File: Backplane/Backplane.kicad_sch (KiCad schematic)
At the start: 33 parts, among them J10 Conn_01x02, J11 Conn_01x02, J12 Conn_02x12_Odd_Even, J13 Conn_01x02, J14 Conn_01x02, J15 Conn_01x02, J16 Conn_01x02, J17 Conn_01x02, J18 Conn_01x02, J19 Conn_01x02_Pin, J20 Conn_01x02_Pin, J21 Conn_01x02_Pin, J22 Conn_01x02_Pin, J23 Conn_01x02_Pin, J24 Conn_01x02_Pin, J25 Conn_01x02_Pin, J26 Conn_01x02_Pin, J27 Conn_01x02, J5 Conn_01x02, J6 1720420202, J7 Conn_01x02, J8 Conn_01x02, J9 Conn_01x02

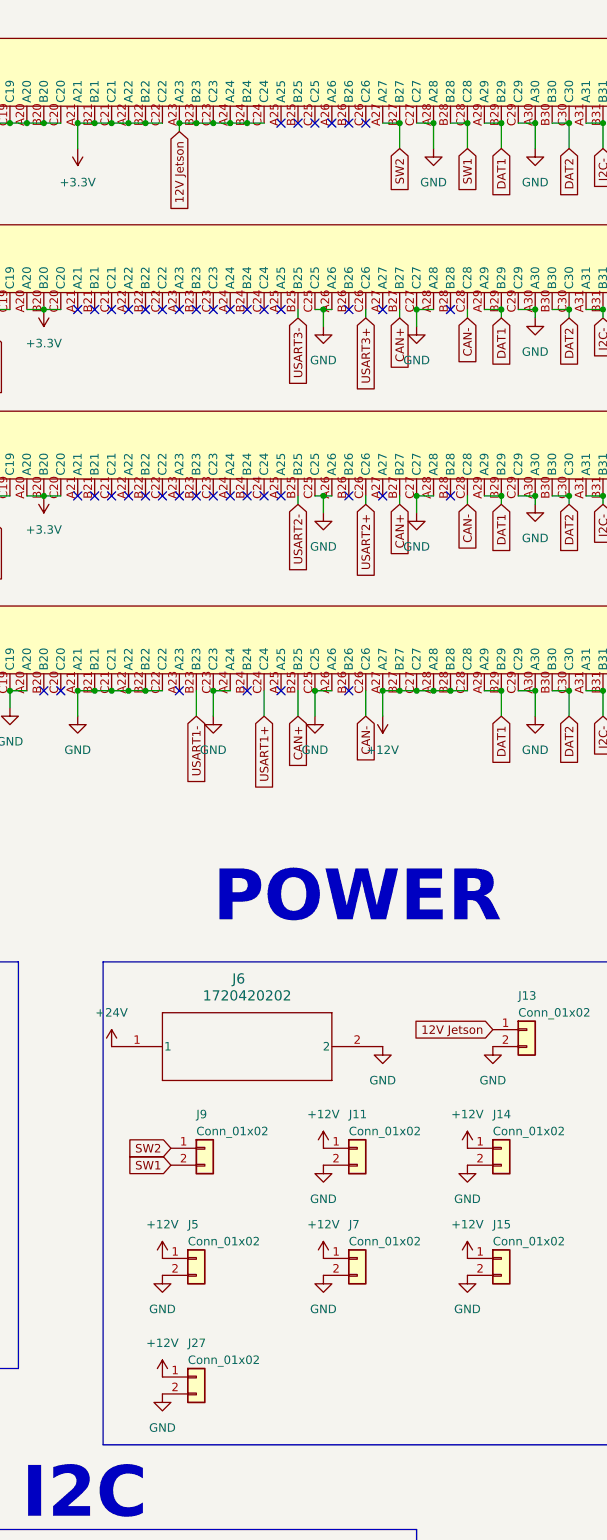
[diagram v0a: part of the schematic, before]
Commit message: Changed Backplane and Power Card for proper connection between the killswitches in the new system
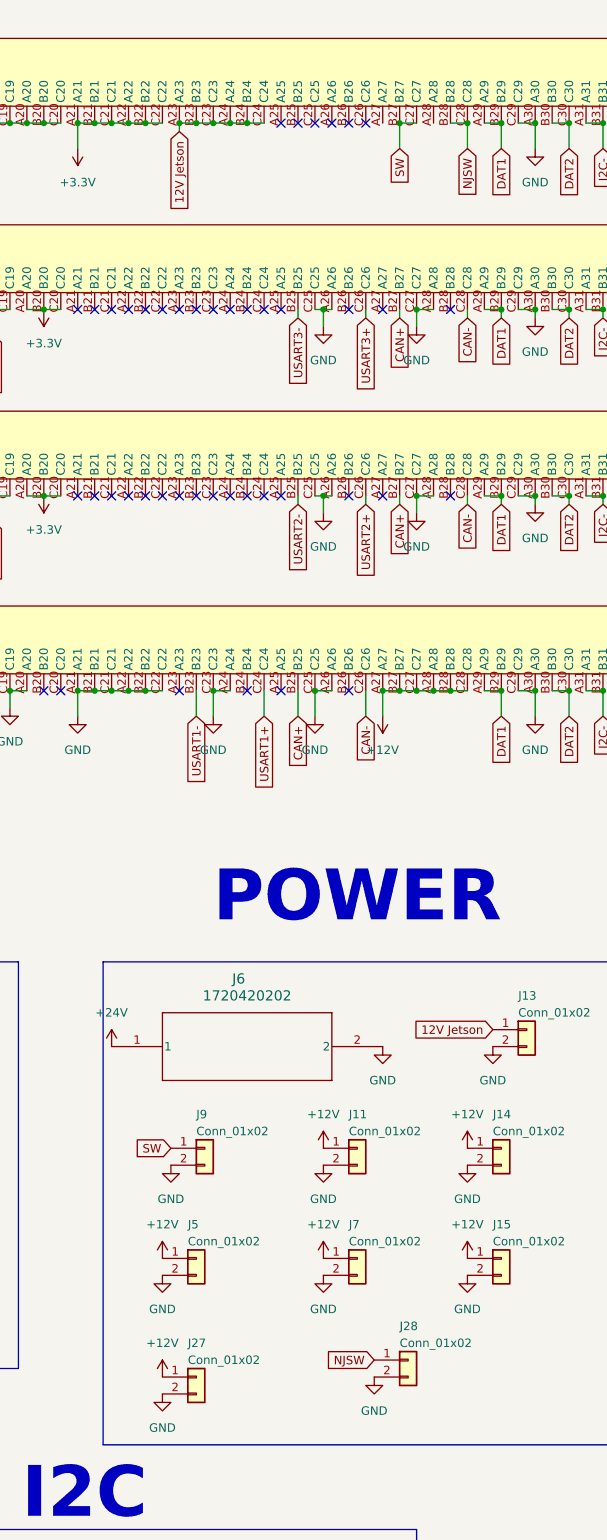
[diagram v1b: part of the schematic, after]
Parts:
- added J28: Conn_01x02, Connector_JST:JST_PH_B2B-PH-K_1x02_P2.00mm_Vertical, symbol Connector_Generic:Conn_01x02
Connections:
- net GND: now also J9.2 (Pin_2), J28.2 (Pin_2); no longer J1.A28, J1.C27
- net SW1 renamed NJSW
- net NJSW: now also J28.1 (Pin_1); no longer J9.2 (Pin_2)
- net SW2 renamed SW
- net SW: now also J1.C27; no longer J1.A27
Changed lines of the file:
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@@
 	)
 	(junction
-		(at 232.41 34.29)
-		(diameter 0)
-		(color 0 0 0 0)
-	)
-	(junction
 		(at 80.01 62.23)
 		(diameter 0)
@@
 	)
 	(junction
+		(at 232.41 34.29)
+		(diameter 0)
+		(color 0 0 0 0)
+	)
+	(junction
 		(at 273.05 62.23)
 		(diameter 0)
@@
 	)
 	(junction
-		(at 237.49 34.29)
-		(diameter 0)
-		(color 0 0 0 0)
-	)
-	(junction
 		(at 209.55 34.29)
 		(diameter 0)
@@
 	(wire
 		(pts
-			(xy 229.87 34.29) (xy 232.41 34.29)
-		)
-		(stroke
-			(width 0)
-			(type default)
-		)
-	)
-	(wire
-		(pts
 			(xy 95.25 90.17) (xy 97.79 90.17)
 		)
@@
 	(wire
 		(pts
-			(xy 234.95 34.29) (xy 237.49 34.29)
-		)
-		(stroke
-			(width 0)
-			(type default)
-		)
-	)
-	(wire
-		(pts
 			(xy 57.15 34.29) (xy 59.69 34.29)
 		)
@@
 	(wire
 		(pts
-			(xy 237.49 34.29) (xy 237.49 38.1)
-		)
-		(stroke
-			(width 0)
-			(type default)
-		)
-	)
-	(wire
-		(pts
 			(xy 295.91 195.58) (xy 297.18 195.58)
 		)
@@
 	(wire
 		(pts
+			(xy 232.41 34.29) (xy 234.95 34.29)
+		)
+		(stroke
+			(width 0)
+			(type default)
+		)
+	)
+	(wire
+		(pts
 			(xy 59.69 62.23) (xy 62.23 62.23)
 		)
@@
 		)
 	)
-	(global_label "SW1"
+	(global_label "NJSW"
 		(shape input)
 		(at 242.57 38.1 270)
@@
 		)
 		(property "Intersheetrefs" "${INTERSHEET_REFS}"
-			(at 242.57 44.9556 90)
+			(at 242.57 46.0442 90)
 			(effects
 				(font
@@
 		)
 	)
-	(global_label "SW2"
+	(global_label "SW"
 		(shape input)
 		(at 198.12 187.96 180)
@@
 		)
 		(property "Intersheetrefs" "${INTERSHEET_REFS}"
-			(at 191.2644 187.96 0)
+			(at 192.4739 187.96 0)
 			(effects
 				(font
@@
 		)
 	)
-	(global_label "SW1"
-		(shape input)
-		(at 198.12 190.5 180)
-		(fields_autoplaced yes)
-		(effects
-			(font
-				(size 1.27 1.27)
-			)
-			(justify right)
-		)
-		(property "Intersheetrefs" "${INTERSHEET_REFS}"
-			(at 191.2644 190.5 0)
-			(effects
-				(font
-					(size 1.27 1.27)
-				)
-				(justify right)
-				(hide yes)
-			)
-		)
-	)
 	(global_label "I2C-"
 		(shape input)
@@
 		)
 	)
-	(global_label "SW2"
+	(global_label "SW"
 		(shape input)
 		(at 232.41 38.1 270)
@@
 		)
 		(property "Intersheetrefs" "${INTERSHEET_REFS}"
-			(at 232.41 44.9556 90)
+			(at 232.41 43.7461 90)
 			(effects
 				(font
@@
 		)
 	)
+	(global_label "NJSW"
+		(shape input)
+		(at 228.6 219.71 180)
+		(fields_autoplaced yes)
+		(effects
+			(font
+				(size 1.27 1.27)
+			)
+			(justify right)
+		)
+		(property "Intersheetrefs" "${INTERSHEET_REFS}"
+			(at 220.6558 219.71 0)
+			(effects
+				(font
+					(size 1.27 1.27)
+				)
+				(justify right)
+				(hide yes)
+			)
+		)
+	)
 	(global_label "DAT2"
 		(shape input)
@@
 	)
 	(symbol
-		(lib_id "power:GND")
-		(at 237.49 38.1 0)
-		(unit 1)
-		(exclude_from_sim no)
-		(in_bom yes)
-		(on_board yes)
-		(dnp no)
-		(fields_autoplaced yes)
-		(property "Reference" "#PWR038"
-			(at 237.49 44.45 0)
-			(effects
-				(font
-					(size 1.27 1.27)
-				)
-				(hide yes)
-			)
-		)
-		(property "Value" "GND"
-			(at 237.49 43.18 0)
-			(effects
-				(font
-					(size 1.27 1.27)
-				)
-			)
-		)
-		(property "Footprint" ""
-			(at 237.49 38.1 0)
-			(effects
-				(font
-					(size 1.27 1.27)
-				)
-				(hide yes)
-			)
-		)
-		(property "Datasheet" ""
-			(at 237.49 38.1 0)
-			(effects
-				(font
-					(size 1.27 1.27)
-				)
-				(hide yes)
-			)
-		)
-		(property "Description" ""
-			(at 237.49 38.1 0)
-			(effects
-				(font
-					(size 1.27 1.27)
-				)
-				(hide yes)
-			)
-		)
-		(pin "1"
-		)
-		(instances
-			(project "Backplane"
-				(path "/73356aaf-05d8-4115-a1e4-2bd56b8d572b"
-					(reference "#PWR038")
-					(unit 1)
-				)
-			)
-		)
-	)
-	(symbol
 		(lib_name "GND_1")
 		(lib_id "power:GND")
@@
 	)
 	(symbol
+		(lib_name "GND_2")
+		(lib_id "power:GND")
+		(at 198.12 190.5 0)
+		(unit 1)
+		(exclude_from_sim no)
+		(in_bom yes)
+		(on_board yes)
+		(dnp no)
+		(fields_autoplaced yes)
+		(property "Reference" "#PWR069"
+			(at 198.12 196.85 0)
+			(effects
+				(font
+					(size 1.27 1.27)
+				)
+				(hide yes)
+			)
+		)
+		(property "Value" "GND"
+			(at 198.12 195.58 0)
+			(effects
+				(font
+					(size 1.27 1.27)
+				)
+			)
+		)
+		(property "Footprint" ""
+			(at 198.12 190.5 0)
+			(effects
+				(font
+					(size 1.27 1.27)
+				)
+				(hide yes)
+			)
+		)
+		(property "Datasheet" ""
+			(at 198.12 190.5 0)
+			(effects
+				(font
+					(size 1.27 1.27)
+				)
+				(hide yes)
+			)
+		)
+		(property "Description" "Power symbol creates a global label with name \"GND\" , ground"
+			(at 198.12 190.5 0)
+			(effects
+				(font
+					(size 1.27 1.27)
+				)
+				(hide yes)
+			)
+		)
+		(pin "1"
+		)
+		(instances
+			(project ""
+				(path "/73356aaf-05d8-4115-a1e4-2bd56b8d572b"
+					(reference "#PWR069")
+					(unit 1)
+				)
+			)
+		)
+	)
+	(symbol
 		(lib_id "power:+12V")
 		(at 31.75 66.04 180)
@@
 	)
 	(symbol
+		(lib_id "Connector_Generic:Conn_01x02")
+		(at 233.68 219.71 0)
+		(unit 1)
+		(exclude_from_sim no)
+		(in_bom yes)
+		(on_board yes)
+		(dnp no)
+		(property "Reference" "J28"
+			(at 232.41 214.63 0)
+			(effects
+				(font
+					(size 1.27 1.27)
+				)
+				(justify left)
+			)
+		)
+		(property "Value" "Conn_01x02"
+			(at 232.41 217.17 0)
+			(effects
+				(font
+					(size 1.27 1.27)
+				)
+				(justify left)
+			)
+		)
+		(property "Footprint" "Connector_JST:JST_PH_B2B-PH-K_1x02_P2.00mm_Vertical"
+			(at 233.68 219.71 0)
+			(effects
+				(font
+					(size 1.27 1.27)
+				)
+				(hide yes)
+			)
+		)
+		(property "Datasheet" "~"
+			(at 233.68 219.71 0)
+			(effects
+				(font
+					(size 1.27 1.27)
+				)
+				(hide yes)
+			)
+		)
+		(property "Description" ""
+			(at 233.68 219.71 0)
+			(effects
+				(font
+					(size 1.27 1.27)
+				)
+				(hide yes)
+			)
+		)
+		(pin "1"
+		)
+		(pin "2"
+		)
+		(instances
+			(project "Backplane"
+				(path "/73356aaf-05d8-4115-a1e4-2bd56b8d572b"
+					(reference "J28")
+					(unit 1)
+				)
+			)
+		)
+	)
+	(symbol
 		(lib_id "Connector:Conn_01x02_Pin")
 		(at 153.67 172.72 0)
@@
 					(unit 1)
 				)
+			)
+		)
+	)
+	(symbol
+		(lib_name "GND_2")
+		(lib_id "power:GND")
+		(at 228.6 222.25 0)
+		(unit 1)
+		(exclude_from_sim no)
+		(in_bom yes)
+		(on_board yes)
+		(dnp no)
+		(fields_autoplaced yes)
+		(property "Reference" "#PWR070"
+			(at 228.6 228.6 0)
+			(effects
+				(font
+					(size 1.27 1.27)
+				)
+				(hide yes)
+			)
+		)
+		(property "Value" "GND"
+			(at 228.6 227.33 0)
+			(effects
+				(font
+					(size 1.27 1.27)
+				)
+			)
+		)
+		(property "Footprint" ""
+			(at 228.6 222.25 0)
+			(effects
+				(font
+					(size 1.27 1.27)
+				)
+				(hide yes)
+			)
+		)
+		(property "Datasheet" ""
+			(at 228.6 222.25 0)
+			(effects
+				(font
+					(size 1.27 1.27)
+				)
+				(hide yes)
+			)
+		)
+		(property "Description" "Power symbol creates a global label with name \"GND\" , ground"
+			(at 228.6 222.25 0)
+			(effects
+				(font
+					(size 1.27 1.27)
+				)
+				(hide yes)
+			)
+		)
+		(pin "1"
+		)
+		(instances
+			(project "Backplane"
+				(path "/73356aaf-05d8-4115-a1e4-2bd56b8d572b"
+					(reference "#PWR070")
+					(unit 1)
+				)

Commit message: Added Silkscreen & Backplane Integration
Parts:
- added R3, R4: 4.7k, Resistor_SMD:R_0805_2012Metric, symbol Device:R_US
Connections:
- net +3.3V: now also R3.1, R4.1
- net I2CJetson+: now also R3.2
- net I2CJetson-: now also R4.2
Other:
- note added: "Miscellaneous Card"
- note added: "Thruster Card 1"
- note added: "Thruster Card 2"
- note removed: "ESC Card 1"
- note removed: "ESC Card 2"
- note removed: "Ethernet/peripheral card"
- moved on the sheet: J25, J26

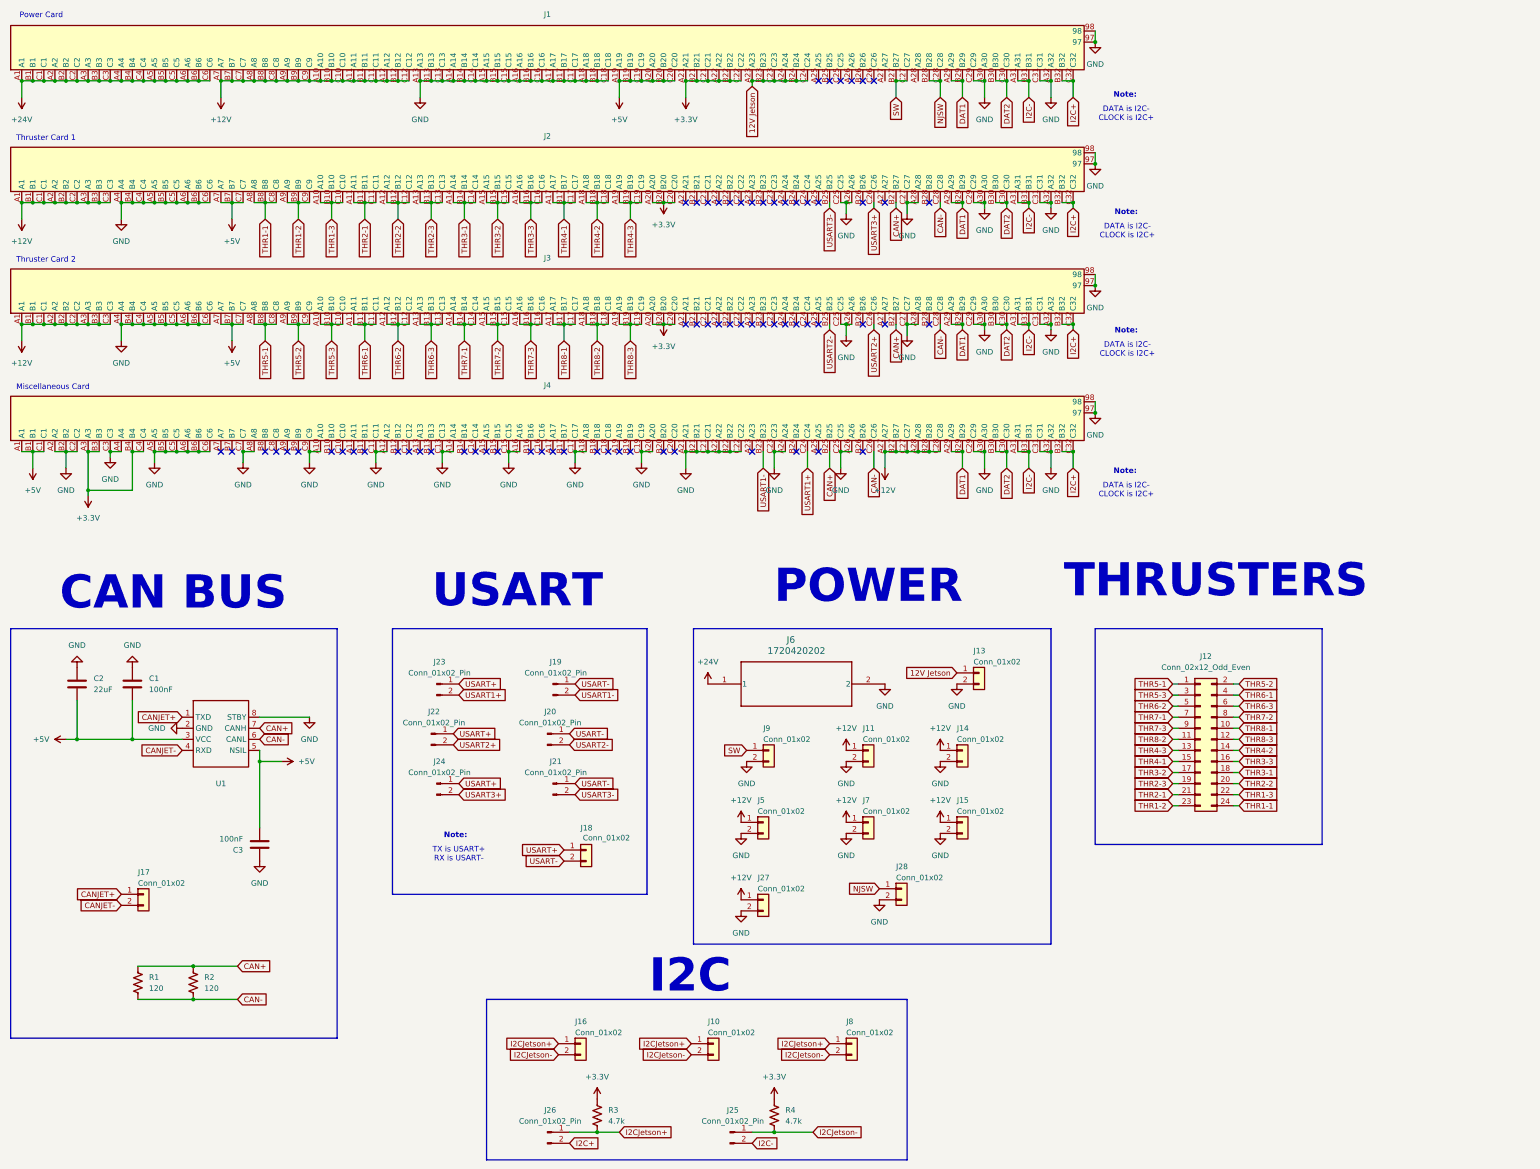
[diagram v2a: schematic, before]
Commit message: Added More Connectors to Backplane
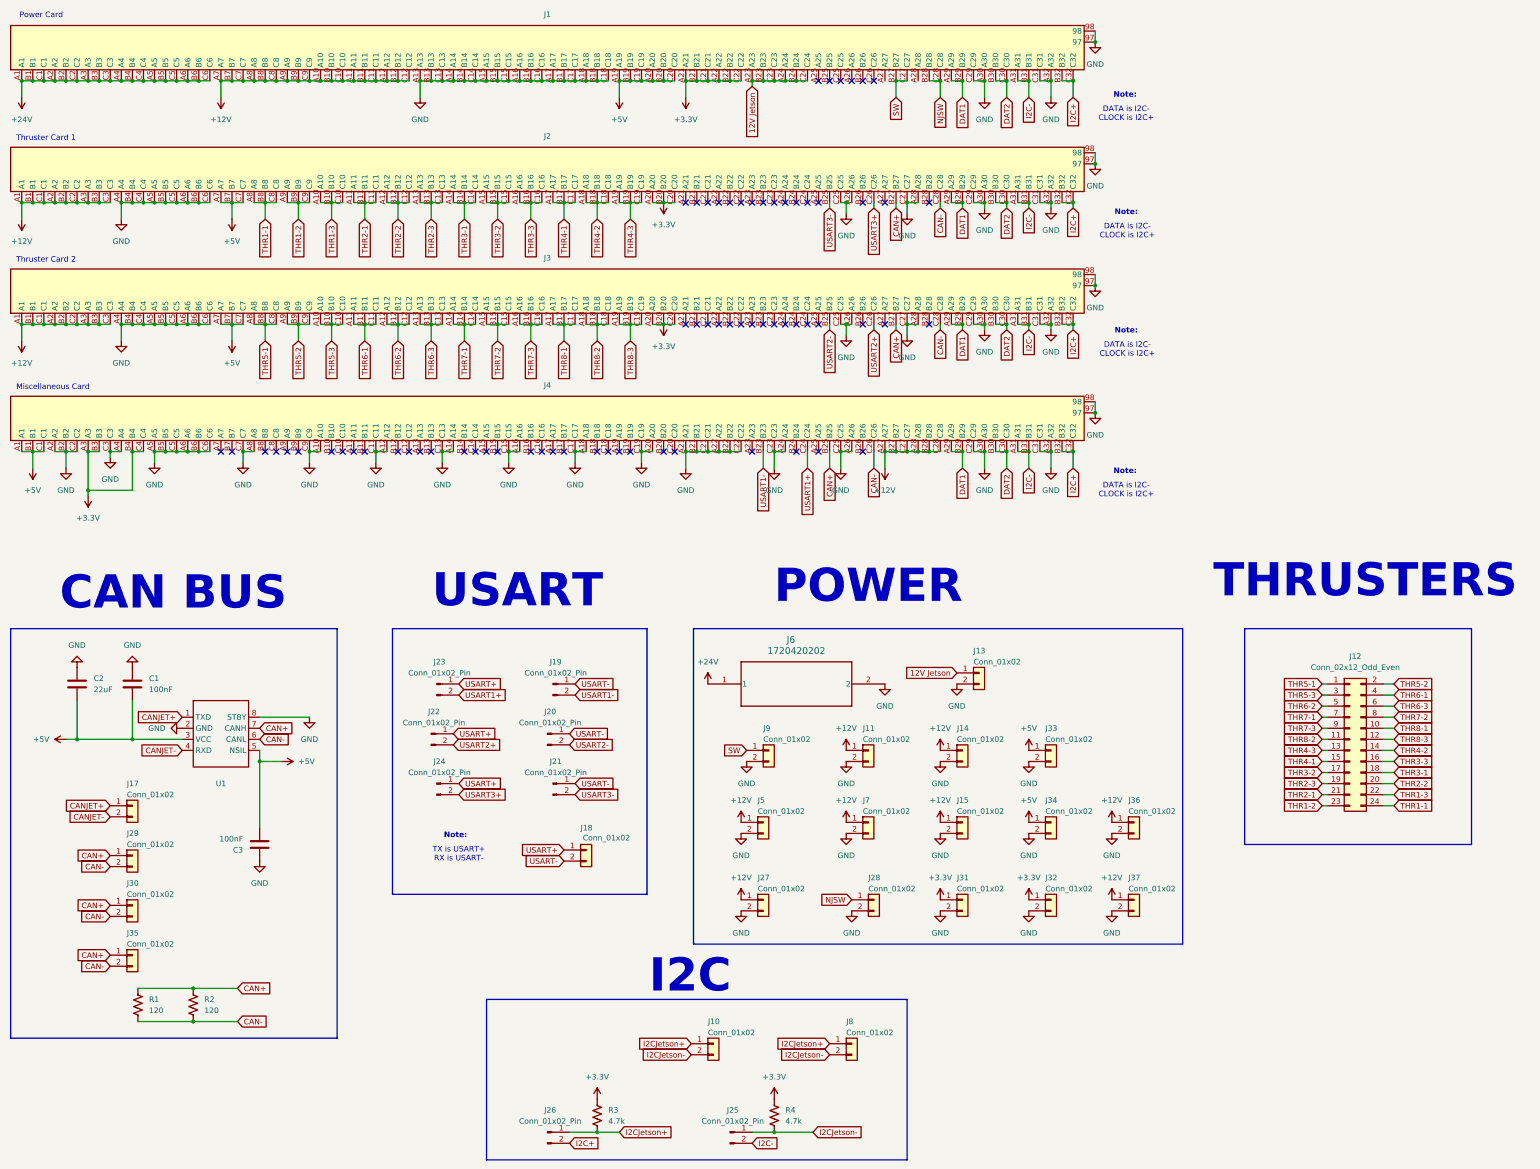
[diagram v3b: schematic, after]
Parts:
- removed J16: Conn_01x02, Connector_JST:JST_PH_B2B-PH-K_1x02_P2.00mm_Vertical, symbol Connector_Generic:Conn_01x02
- added J29, J30, J31, J32, J33, J34, J35, J36, J37: Conn_01x02, Connector_JST:JST_PH_B2B-PH-K_1x02_P2.00mm_Vertical, symbol Connector_Generic:Conn_01x02
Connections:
- net +12V: now also J36.1 (Pin_1), J37.1 (Pin_1)
- net +3.3V: now also J31.1 (Pin_1), J32.1 (Pin_1)
- net +5V: now also J33.1 (Pin_1), J34.1 (Pin_1)
- net CAN+: now also J29.1 (Pin_1), J30.1 (Pin_1), J35.1 (Pin_1)
- net CAN-: now also J29.2 (Pin_2), J30.2 (Pin_2), J35.2 (Pin_2)
- net GND: now also J31.2 (Pin_2), J32.2 (Pin_2), J33.2 (Pin_2), J34.2 (Pin_2), J36.2 (Pin_2), J37.2 (Pin_2)
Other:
- moved on the sheet: J12, J17, J28, R1, R2
